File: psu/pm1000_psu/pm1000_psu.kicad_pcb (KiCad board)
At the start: 2 copper layers, 105 x 35 mm, 42 parts, among them J1 , J2 , J3 , J4 , J5 , U1 LM317_TO-220, U2 LM317_TO-220, U3 LM317_TO-220

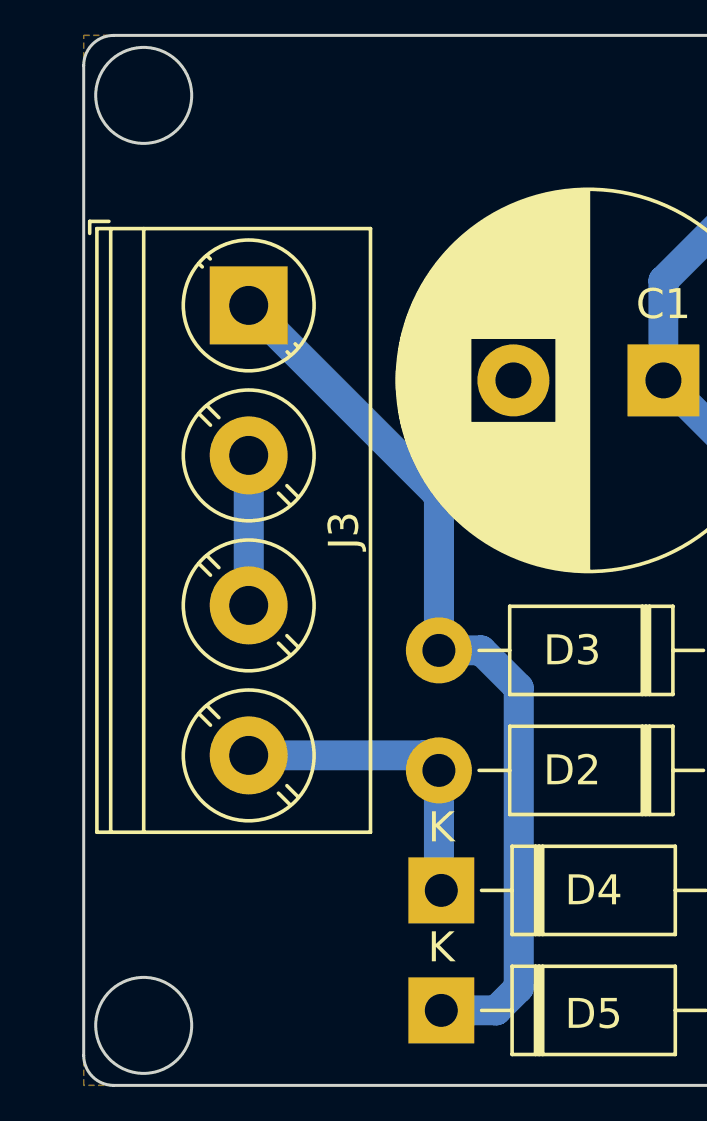
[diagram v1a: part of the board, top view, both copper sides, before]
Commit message: set led resistors to 22k, place new psu terminal block
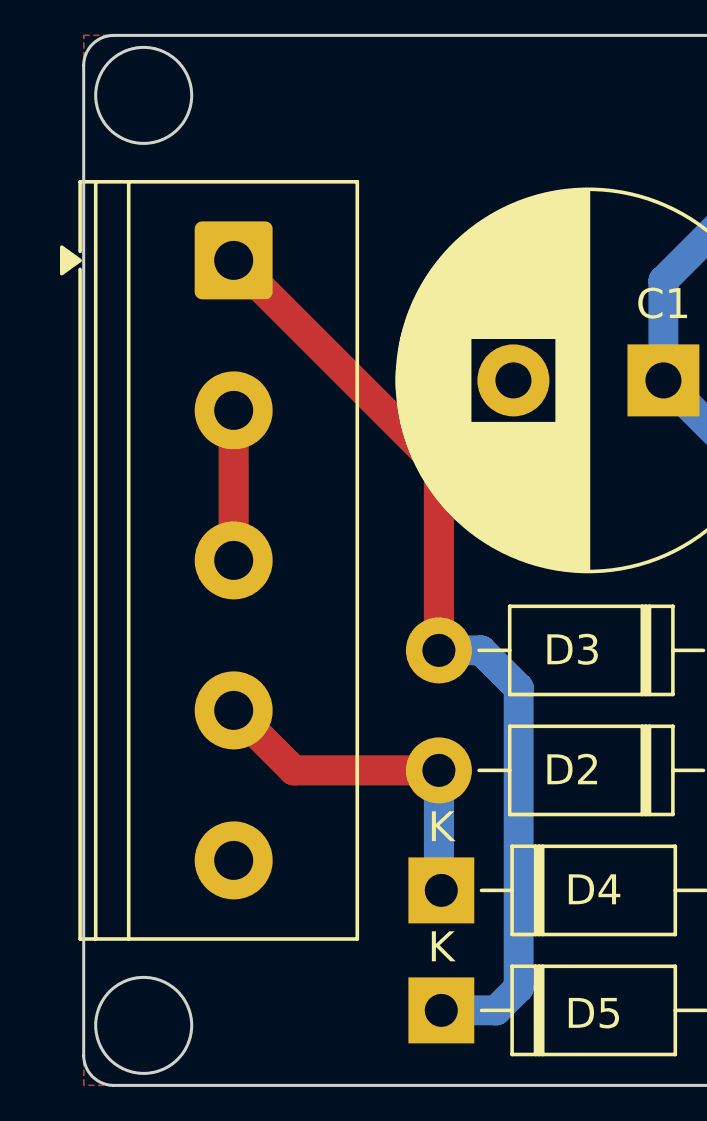
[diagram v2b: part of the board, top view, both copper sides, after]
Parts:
- C1: value 200uF 80V -> 220uF 80V
- C3, C6, C8: value 10uF 63V -> 10uF 80V
- J1, J2, J4, J5: value (none) -> ~
- J3: value (none) -> Screw_Terminal_01x05; footprint TerminalBlock_Phoenix:TerminalBlock_Phoenix_PT-1,5-4-5.0-H_1x04_P5.00mm_Horizontal -> TerminalBlock_Phoenix:TerminalBlock_Phoenix_PT-1,5-5-5.0-H_1x05_P5.00mm_Horizontal
- R10, R11, R12, R2: value 2k2 -> 22k
- moved J3 1.58 mm to (25.0, 37.5)
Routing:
- net Net-(D3-A): track 30.2 -> 31.9 mm
- net Net-(D2-A): track 10.6 -> 11.7 mm
